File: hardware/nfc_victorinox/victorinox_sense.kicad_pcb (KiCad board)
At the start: 4 copper layers, 14.6 x 38.6 mm, 24 parts, among them U1 TMP117AIDRVR, U2 RF430CL330HIRGTR‎, U3 ATtiny1626-MFR

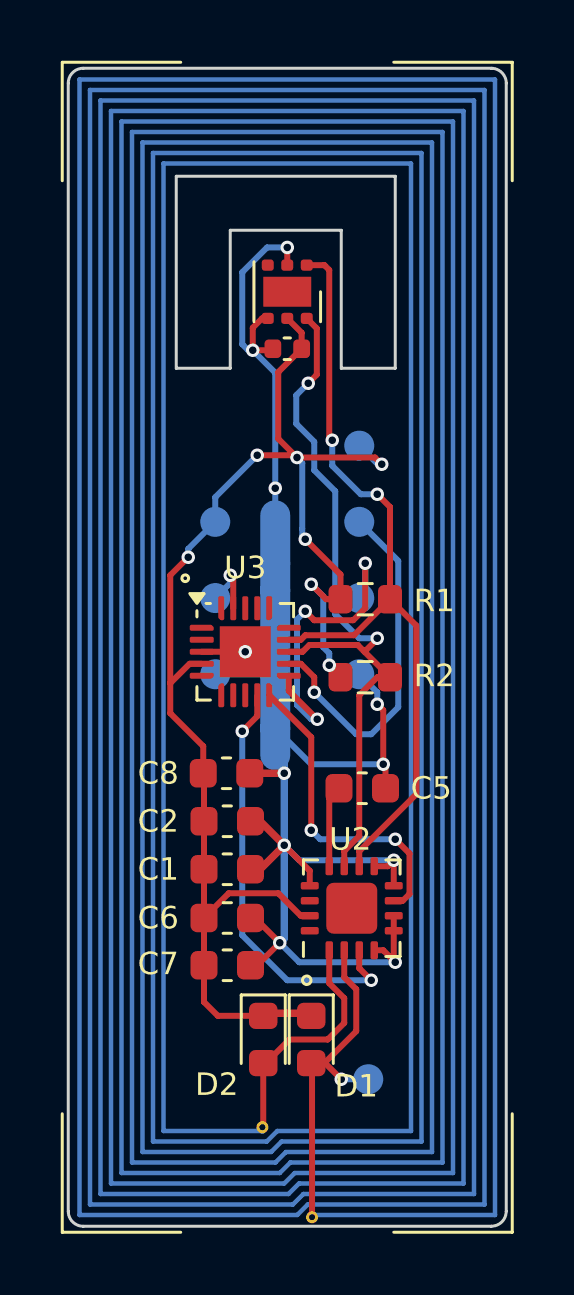
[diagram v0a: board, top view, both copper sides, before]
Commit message: switch antenna layer
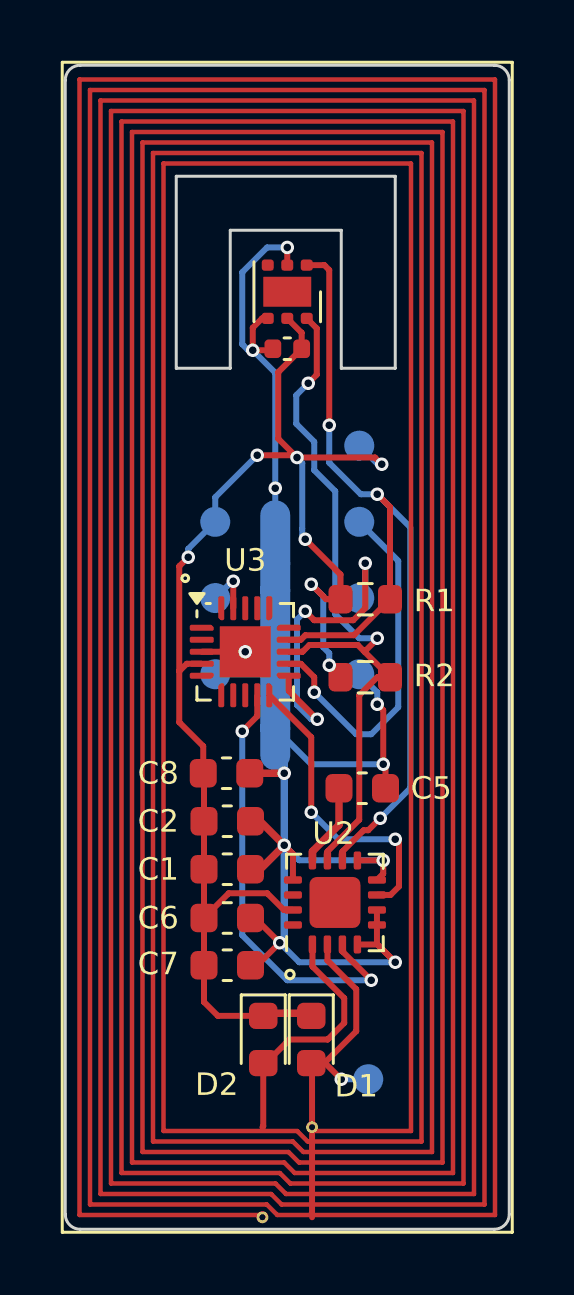
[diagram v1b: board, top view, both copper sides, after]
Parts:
- AE1: moved to F.Cu
- moved AE1 14.0 mm to (122.5, 32.8), turned to 0 degrees
- moved U2 0.59 mm to (131.1, 60.3)
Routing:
- net SCL: track 26.9 -> 30.6 mm, vias 2 -> 3
- net VCC: track 50.1 -> 48.7 mm
- net RF430_INT: track 10.6 -> 10.1 mm
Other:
- board size 14.6 x 38.6 mm -> 14.8 x 38.8 mm

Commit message: flip antenna layer, fix ANT connection issues
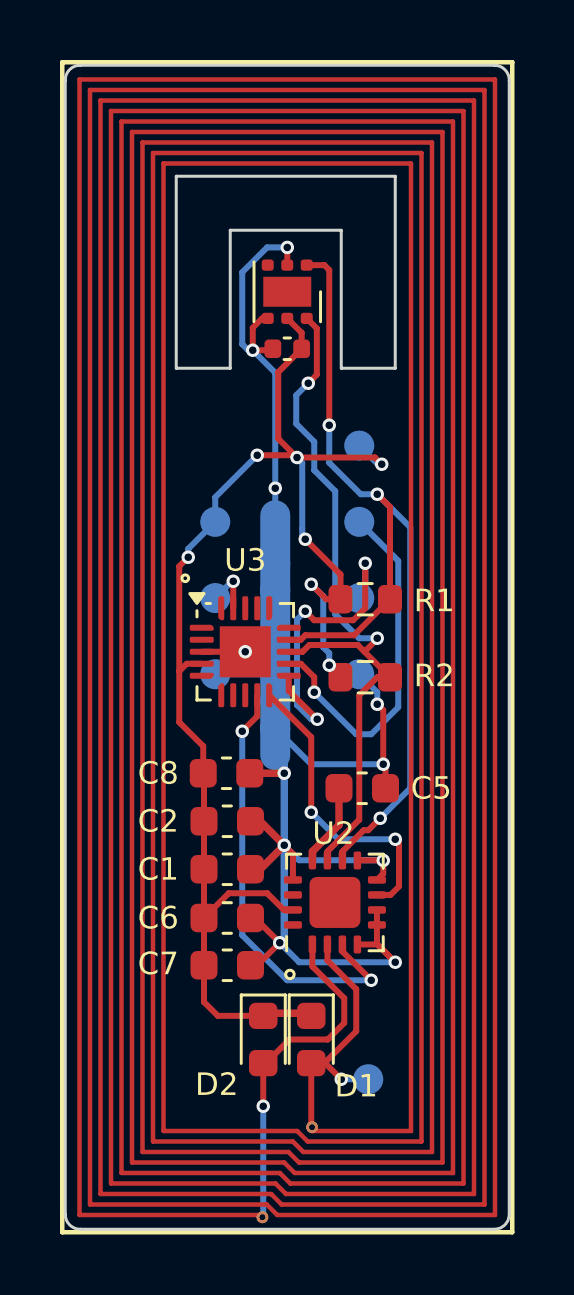
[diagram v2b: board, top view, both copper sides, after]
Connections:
- AE1 pad 1: ANT2 -> ANT1
- AE1 pad 2: ANT1 -> ANT2
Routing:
- net ANT2: track 12.5 -> 9.50 mm
- net ANT1: track 8.49 -> 11.5 mm, vias 0 -> 1
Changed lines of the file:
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@@
 		(attr through_hole)
 		(fp_line
-			(start 6.172614 38)
-			(end 6.172614 37.925)
+			(start 6.172614 37.925)
+			(end 6.172614 38)
 			(stroke
-				(width 0.2)
+				(width 0.12)
 				(type default)
 			)
 			(layer "F.Cu")
-			(net 2)
 		)
 		(fp_line
@@
 			(end 7.827386 35)
 			(stroke
-				(width 0.2)
+				(width 0.12)
 				(type default)
 			)
 			(layer "F.Cu")
-			(net 3)
 		)
 		(fp_line
@@
 			(end -0.5 3.45)
 			(stroke
-				(width 0.1)
+				(width 0.15)
 				(type solid)
 			)
@@
 			(end 3.45 -0.5)
 			(stroke
-				(width 0.1)
+				(width 0.15)
 				(type solid)
 			)
@@
 			(end -0.5 34.55)
 			(stroke
-				(width 0.1)
+				(width 0.15)
 				(type solid)
 			)
@@
 			(end 3.45 38.5)
 			(stroke
-				(width 0.1)
+				(width 0.15)
 				(type solid)
 			)
@@
 			(end 10.55 -0.5)
 			(stroke
-				(width 0.1)
+				(width 0.15)
 				(type solid)
 			)
@@
 			(end 14.5 3.45)
 			(stroke
-				(width 0.1)
+				(width 0.15)
 				(type solid)
 			)
@@
 			(end 10.55 38.5)
 			(stroke
-				(width 0.1)
+				(width 0.15)
 				(type solid)
 			)
@@
 			(end 14.5 34.55)
 			(stroke
-				(width 0.1)
+				(width 0.15)
 				(type solid)
 			)
@@
 			(end 14.5 -0.5)
 			(stroke
-				(width 0.1)
+				(width 0.15)
 				(type solid)
 			)
@@
 			(end -0.5 -0.5)
 			(stroke
-				(width 0.1)
+				(width 0.15)
 				(type solid)
 			)
@@
 			(end 14.5 38.5)
 			(stroke
-				(width 0.1)
+				(width 0.15)
 				(type solid)
 			)
@@
 			(end -0.5 38.5)
 			(stroke
-				(width 0.1)
+				(width 0.15)
 				(type solid)
 			)
@@
 			(size 0.15 0.15)
 			(layers "F.Cu")
-			(net 2 "ANT2")
+			(net 3 "ANT1")
 			(pintype "input")
 			(zone_connect 0)
@@
 			(layers "*.Cu" "*.Mask")
 			(remove_unused_layers no)
-			(net 2 "ANT2")
+			(net 3 "ANT1")
 			(pintype "input")
 		)
@@
 			(layers "*.Cu" "*.Mask")
 			(remove_unused_layers no)
-			(net 3 "ANT1")
+			(net 2 "ANT2")
 			(pintype "input")
 		)
@@
 			(size 0.15 0.15)
 			(layers "F.Cu")
-			(net 3 "ANT1")
+			(net 2 "ANT2")
 			(pintype "input")
 			(zone_connect 0)
@@
 	)
 	(segment
-		(start 130.327386 65.689886)
-		(end 130.3 65.6625)
-		(width 0.2)
-		(layer "F.Cu")
-		(net 2)
-	)
-	(segment
 		(start 130.3 65.6625)
 		(end 130.7625 65.6625)
@@
 	)
 	(segment
-		(start 130.327386 70.8)
-		(end 130.327386 65.689886)
+		(start 130.7625 65.6625)
+		(end 131.3 66.2)
 		(width 0.2)
 		(layer "F.Cu")
@@
 	)
 	(segment
-		(start 130.7625 65.6625)
-		(end 131.3 66.2)
+		(start 131.8 63.2)
+		(end 131.8 64.6)
 		(width 0.2)
 		(layer "F.Cu")
@@
 	)
 	(segment
-		(start 131.8 63.2)
-		(end 131.8 64.6)
+		(start 130.3 65.6625)
+		(end 130.3 67.772614)
 		(width 0.2)
 		(layer "F.Cu")
@@
 	)
 	(segment
-		(start 130.3 70.700001)
-		(end 130.327386 70.700001)
+		(start 130.3 67.772614)
+		(end 130.327386 67.8)
 		(width 0.2)
 		(layer "F.Cu")
@@
 	)
 	(segment
-		(start 128.7 65.6625)
-		(end 128.7 67.772614)
-		(width 0.2)
-		(layer "F.Cu")
-		(net 3)
-	)
-	(segment
 		(start 128.622614 65.422614)
 		(end 128.6 65.4)
@@
 	)
 	(segment
-		(start 128.7 67.772614)
-		(end 128.672614 67.8)
+		(start 128.7 65.6625)
+		(end 128.7 67.1)
 		(width 0.2)
 		(layer "F.Cu")
@@
 		(net 3)
 	)
+	(via
+		(at 128.7 67.1)
+		(size 0.45)
+		(drill 0.25)
+		(layers "F.Cu" "B.Cu")
+		(net 3)
+	)
+	(segment
+		(start 128.7 70.772614)
+		(end 128.672614 70.8)
+		(width 0.2)
+		(layer "B.Cu")
+		(net 3)
+	)
+	(segment
+		(start 128.7 67.1)
+		(end 128.7 70.772614)
+		(width 0.2)
+		(layer "B.Cu")
+		(net 3)
+	)
